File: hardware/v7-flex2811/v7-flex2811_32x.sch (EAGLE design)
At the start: 160 parts

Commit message: Rebuild a 32 strip from the slightly update single
Single has more room to place passives and slightly smaller
2818 pads so that there's more clearance with the edge
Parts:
- removed IN1: 4PAD, Sparky:4PAD
- added C21, C22, C23, C24, C25, C26, C27, C28, C29, C30, C31, C32: (no value), rcl:C-EUC0201
- added R61, R62, R63, R64, R65, R66, R67, R68, R69, R70, R71, R72, R73, R74, R75, R76, R77, R78, R79, R80, R81, R82, R83, R84, R85, R86, R87, R88, R89, R90, R91, R92, R93, R94, R95, R96: (no value), rcl:R-US_R0201
- added U$100, U$103, U$104, U$107, U$108, U$111, U$112, U$115, U$116, U$119, U$120, U$123, U$124, U$127, U$128, U$3, U$83, U$84, U$87, U$88, U$91, U$92, U$95, U$96, U$99: 4PAD, Sparky:4PAD
- added U$101, U$105, U$109, U$113, U$117, U$121, U$125, U$81, U$85, U$89, U$93, U$97: TP_4MM_MED_PAD, tom-tappytap-v5-flex:TP_4MM_MED_PAD
- added U$102, U$106, U$110, U$114, U$118, U$122, U$126, U$82, U$86, U$90, U$94, U$98: WS2818, Sparky:WS2818
- U$10, U$14, U$18, U$2, U$22, U$26, U$30, U$34, U$38, U$42, U$46, U$50, U$54, U$58, U$6, U$62, U$66, U$70, U$74, U$78: device adafruit:WS2818 -> Sparky:WS2818
- renumbered OUT1 to U$4
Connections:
- removed net BIN1: IN1.BIN, U$2.BIN
- removed net DIN1: IN1.DIN, R4.2, U$4.BIN, U$6.BIN, U$7.BIN
- new net BIN0: U$2.BIN, U$3.P$2
- new net DIN0: R4.2, U$3.P$1, U$4.P$2, U$6.BIN, U$7.P$2
- new net DOUT0: R1.2, R5.1, U$10.BIN, U$11.P$2, U$4.P$1, U$7.P$1, U$8.P$2
- new net DOUT21: R65.1, R67.2, U$88.P$1, U$91.P$1, U$92.P$2, U$94.BIN, U$95.P$2
- new net DOUT22: R68.1, R70.2, U$92.P$1, U$95.P$1, U$96.P$2, U$98.BIN, U$99.P$2
- new net DOUT23: R71.1, R73.2, U$100.P$2, U$102.BIN, U$103.P$2, U$96.P$1, U$99.P$1
- new net DOUT24: R74.1, R76.2, U$100.P$1, U$103.P$1, U$104.P$2, U$106.BIN, U$107.P$2
- new net DOUT25: R77.1, R79.2, U$104.P$1, U$107.P$1, U$108.P$2, U$110.BIN, U$111.P$2
- new net DOUT26: R80.1, R82.2, U$108.P$1, U$111.P$1, U$112.P$2, U$114.BIN, U$115.P$2
- new net DOUT27: R83.1, R85.2, U$112.P$1, U$115.P$1, U$116.P$2, U$118.BIN, U$119.P$2
- new net DOUT28: R86.1, R88.2, U$116.P$1, U$119.P$1, U$120.P$2, U$122.BIN, U$123.P$2
- new net DOUT29: R89.1, R91.2, U$120.P$1, U$123.P$1, U$124.P$2, U$126.BIN, U$127.P$2
- new net DOUT30: R92.1, R94.2, U$124.P$1, U$127.P$1, U$128.P$2
- new net DOUT31: R95.1, U$128.P$1
- new net N$61: R61.1, U$82.DIN
- new net N$62: R62.2, U$82.DO
- new net N$63: R63.1, U$82.VDD
- new net N$64: R64.1, U$86.DIN
- new net N$65: R65.2, U$86.DO
- new net N$66: R66.1, U$86.VDD
- new net N$67: R67.1, U$90.DIN
- new net N$68: R68.2, U$90.DO
- new net N$69: R69.1, U$90.VDD
- new net N$70: R70.1, U$94.DIN
- new net N$71: R71.2, U$94.DO
- new net N$72: R72.1, U$94.VDD
- new net N$73: R73.1, U$98.DIN
- new net N$74: R74.2, U$98.DO
- new net N$75: R75.1, U$98.VDD
- new net N$76: R76.1, U$102.DIN
- new net N$77: R77.2, U$102.DO
- new net N$78: R78.1, U$102.VDD
- new net N$79: R79.1, U$106.DIN
- new net N$80: R80.2, U$106.DO
- new net N$81: R81.1, U$106.VDD
- new net N$82: R82.1, U$110.DIN
- new net N$83: R83.2, U$110.DO
- new net N$84: R84.1, U$110.VDD
- new net N$85: R85.1, U$114.DIN
- new net N$86: R86.2, U$114.DO
- new net N$87: R87.1, U$114.VDD
- new net N$88: R88.1, U$118.DIN
- new net N$89: R89.2, U$118.DO
- new net N$90: R90.1, U$118.VDD
- new net N$91: R91.1, U$122.DIN
- new net N$92: R92.2, U$122.DO
- new net N$93: R93.1, U$122.VDD
- new net N$94: R94.1, U$126.DIN
- new net N$95: R95.2, U$126.DO
- new net N$96: R96.1, U$126.VDD
- new net NEG_PAD0: U$1.0, U$2.OUTB, U$2.OUTG, U$2.OUTR
- new net NEG_PAD21: U$85.0, U$86.OUTB, U$86.OUTG, U$86.OUTR
- new net NEG_PAD22: U$89.0, U$90.OUTB, U$90.OUTG, U$90.OUTR
- new net NEG_PAD23: U$93.0, U$94.OUTB, U$94.OUTG, U$94.OUTR
- new net NEG_PAD24: U$97.0, U$98.OUTB, U$98.OUTG, U$98.OUTR
- new net NEG_PAD25: U$101.0, U$102.OUTB, U$102.OUTG, U$102.OUTR
- new net NEG_PAD26: U$105.0, U$106.OUTB, U$106.OUTG, U$106.OUTR
- new net NEG_PAD27: U$109.0, U$110.OUTB, U$110.OUTG, U$110.OUTR
- new net NEG_PAD28: U$113.0, U$114.OUTB, U$114.OUTG, U$114.OUTR
- new net NEG_PAD29: U$117.0, U$118.OUTB, U$118.OUTG, U$118.OUTR
- new net NEG_PAD30: U$121.0, U$122.OUTB, U$122.OUTG, U$122.OUTR
- new net NEG_PAD31: U$125.0, U$126.OUTB, U$126.OUTG, U$126.OUTR
- net DOUT1: now also R2.1, R7.2, U$11.P$1, U$12.P$2, U$14.BIN, U$15.P$2, U$8.P$1; no longer R1.2, R5.1, U$10.BIN, U$11.BIN, U$4.DIN, U$7.DIN, U$8.BIN
- net DOUT10: now also R32.1, R34.2, U$44.P$1, U$47.P$1, U$48.P$2, U$50.BIN, U$51.P$2; no longer R29.1, R31.2, U$40.DIN, U$43.DIN, U$44.BIN, U$46.BIN, U$47.BIN
- net DOUT11: now also R35.1, R37.2, U$48.P$1, U$51.P$1, U$52.P$2, U$54.BIN, U$55.P$2; no longer R32.1, R34.2, U$44.DIN, U$47.DIN, U$48.BIN, U$50.BIN, U$51.BIN
- net DOUT12: now also R38.1, R40.2, U$52.P$1, U$55.P$1, U$56.P$2, U$58.BIN, U$59.P$2; no longer R35.1, R37.2, U$48.DIN, U$51.DIN, U$52.BIN, U$54.BIN, U$55.BIN
- net DOUT13: now also R41.1, R43.2, U$56.P$1, U$59.P$1, U$60.P$2, U$62.BIN, U$63.P$2; no longer R38.1, R40.2, U$52.DIN, U$55.DIN, U$56.BIN, U$58.BIN, U$59.BIN
- net DOUT14: now also R44.1, R46.2, U$60.P$1, U$63.P$1, U$64.P$2, U$66.BIN, U$67.P$2; no longer R41.1, R43.2, U$56.DIN, U$59.DIN, U$60.BIN, U$62.BIN, U$63.BIN
- net DOUT15: now also R47.1, R49.2, U$64.P$1, U$67.P$1, U$68.P$2, U$70.BIN, U$71.P$2; no longer R44.1, R46.2, U$60.DIN, U$63.DIN, U$64.BIN, U$66.BIN, U$67.BIN
- net DOUT16: now also R50.1, R52.2, U$68.P$1, U$71.P$1, U$72.P$2, U$74.BIN, U$75.P$2; no longer R47.1, R49.2, U$64.DIN, U$67.DIN, U$68.BIN, U$70.BIN, U$71.BIN
- net DOUT17: now also R53.1, R55.2, U$72.P$1, U$75.P$1, U$76.P$2, U$78.BIN, U$79.P$2; no longer R50.1, R52.2, U$68.DIN, U$71.DIN, U$72.BIN, U$74.BIN, U$75.BIN
- net DOUT18: now also R56.1, R58.2, U$76.P$1, U$79.P$1, U$80.P$2, U$82.BIN, U$83.P$2; no longer R53.1, R55.2, U$72.DIN, U$75.DIN, U$76.BIN, U$78.BIN, U$79.BIN
- net DOUT19: now also R59.1, R61.2, U$80.P$1, U$83.P$1, U$84.P$2, U$86.BIN, U$87.P$2; no longer R56.1, R58.2, U$76.DIN, U$79.DIN, U$80.BIN
- net DOUT2: now also R10.2, R8.1, U$12.P$1, U$15.P$1, U$16.P$2, U$18.BIN, U$19.P$2; no longer R2.1, R7.2, U$11.DIN, U$12.BIN, U$14.BIN, U$15.BIN, U$8.DIN
- net DOUT20: now also R62.1, R64.2, U$84.P$1, U$87.P$1, U$88.P$2, U$90.BIN, U$91.P$2; no longer R59.1, U$80.DIN
- net DOUT3: now also R11.1, R13.2, U$16.P$1, U$19.P$1, U$20.P$2, U$22.BIN, U$23.P$2; no longer R10.2, R8.1, U$12.DIN, U$15.DIN, U$16.BIN, U$18.BIN, U$19.BIN
- net DOUT4: now also R14.1, R16.2, U$20.P$1, U$23.P$1, U$24.P$2, U$26.BIN, U$27.P$2; no longer R11.1, R13.2, U$16.DIN, U$19.DIN, U$20.BIN, U$22.BIN, U$23.BIN
- net DOUT5: now also R17.1, R19.2, U$24.P$1, U$27.P$1, U$28.P$2, U$30.BIN, U$31.P$2; no longer R14.1, R16.2, U$20.DIN, U$23.DIN, U$24.BIN, U$26.BIN, U$27.BIN
- net DOUT6: now also R20.1, R22.2, U$28.P$1, U$31.P$1, U$32.P$2, U$34.BIN, U$35.P$2; no longer R17.1, R19.2, U$24.DIN, U$27.DIN, U$28.BIN, U$30.BIN, U$31.BIN
- net DOUT7: now also R23.1, R25.2, U$32.P$1, U$35.P$1, U$36.P$2, U$38.BIN, U$39.P$2; no longer R20.1, R22.2, U$28.DIN, U$31.DIN, U$32.BIN, U$34.BIN, U$35.BIN
- net DOUT8: now also R26.1, R28.2, U$36.P$1, U$39.P$1, U$40.P$2, U$42.BIN, U$43.P$2; no longer R23.1, R25.2, U$32.DIN, U$35.DIN, U$36.BIN, U$38.BIN, U$39.BIN
- net DOUT9: now also R29.1, R31.2, U$40.P$1, U$43.P$1, U$44.P$2, U$46.BIN, U$47.P$2; no longer R26.1, R28.2, U$36.DIN, U$39.DIN, U$40.BIN, U$42.BIN, U$43.BIN
- net GND: now also C21.2, C22.2, C23.2, C24.2, C25.2, C26.2, C27.2, C28.2, C29.2, C30.2, C31.2, C32.2, U$100.P$3, U$102.GND, U$103.P$3, U$104.P$3, U$106.GND, U$107.P$3, U$108.P$3, U$11.P$3, U$110.GND, U$111.P$3, U$112.P$3, U$114.GND, U$115.P$3, U$116.P$3, U$118.GND, U$119.P$3, U$12.P$3, U$120.P$3, U$122.GND, U$123.P$3, U$124.P$3, U$126.GND, U$127.P$3, U$128.P$3, U$15.P$3, U$16.P$3, U$19.P$3, U$20.P$3, U$23.P$3, U$24.P$3, U$27.P$3, U$28.P$3, U$3.P$3, U$31.P$3, U$32.P$3, U$35.P$3, U$36.P$3, U$39.P$3, U$4.P$3, U$40.P$3, U$43.P$3, U$44.P$3, U$47.P$3, U$48.P$3, U$51.P$3, U$52.P$3, U$55.P$3, U$56.P$3, U$59.P$3, U$60.P$3, U$63.P$3, U$64.P$3, U$67.P$3, U$68.P$3, U$7.P$3, U$71.P$3, U$72.P$3, U$75.P$3, U$76.P$3, U$79.P$3, U$8.P$3, U$80.P$3, U$82.GND, U$83.P$3, U$84.P$3, U$86.GND, U$87.P$3, U$88.P$3, U$90.GND, U$91.P$3, U$92.P$3, U$94.GND, U$95.P$3, U$96.P$3, U$98.GND, U$99.P$3; no longer IN1.GND, U$11.GND, U$12.GND, U$15.GND, U$16.GND, U$19.GND, U$20.GND, U$23.GND, U$24.GND, U$27.GND, U$28.GND, U$31.GND, U$32.GND, U$35.GND, U$36.GND, U$39.GND, U$4.GND, U$40.GND, U$43.GND, U$44.GND, U$47.GND, U$48.GND, U$51.GND, U$52.GND, U$55.GND, U$56.GND, U$59.GND, U$60.GND, U$63.GND, U$64.GND, U$67.GND, U$68.GND, U$7.GND, U$71.GND, U$72.GND, U$75.GND, U$76.GND, U$79.GND, U$8.GND, U$80.GND
- net NEG_PAD1: now also U$5.0, U$6.OUTB, U$6.OUTG, U$6.OUTR; no longer U$1.0, U$2.OUTB, U$2.OUTG, U$2.OUTR
- net NEG_PAD10: now also U$41.0, U$42.OUTB, U$42.OUTG, U$42.OUTR; no longer U$37.0, U$38.OUTB, U$38.OUTG, U$38.OUTR
- net NEG_PAD11: now also U$45.0, U$46.OUTB, U$46.OUTG, U$46.OUTR; no longer U$41.0, U$42.OUTB, U$42.OUTG, U$42.OUTR
- net NEG_PAD12: now also U$49.0, U$50.OUTB, U$50.OUTG, U$50.OUTR; no longer U$45.0, U$46.OUTB, U$46.OUTG, U$46.OUTR
- net NEG_PAD13: now also U$53.0, U$54.OUTB, U$54.OUTG, U$54.OUTR; no longer U$49.0, U$50.OUTB, U$50.OUTG, U$50.OUTR
- net NEG_PAD14: now also U$57.0, U$58.OUTB, U$58.OUTG, U$58.OUTR; no longer U$53.0, U$54.OUTB, U$54.OUTG, U$54.OUTR
- net NEG_PAD15: now also U$61.0, U$62.OUTB, U$62.OUTG, U$62.OUTR; no longer U$57.0, U$58.OUTB, U$58.OUTG, U$58.OUTR
- net NEG_PAD16: now also U$65.0, U$66.OUTB, U$66.OUTG, U$66.OUTR; no longer U$61.0, U$62.OUTB, U$62.OUTG, U$62.OUTR
- net NEG_PAD17: now also U$69.0, U$70.OUTB, U$70.OUTG, U$70.OUTR; no longer U$65.0, U$66.OUTB, U$66.OUTG, U$66.OUTR
- net NEG_PAD18: now also U$73.0, U$74.OUTB, U$74.OUTG, U$74.OUTR; no longer U$69.0, U$70.OUTB, U$70.OUTG, U$70.OUTR
- net NEG_PAD19: now also U$77.0, U$78.OUTB, U$78.OUTG, U$78.OUTR; no longer U$73.0, U$74.OUTB, U$74.OUTG, U$74.OUTR
- net NEG_PAD2: now also U$10.OUTB, U$10.OUTG, U$10.OUTR, U$9.0; no longer U$5.0, U$6.OUTB, U$6.OUTG, U$6.OUTR
- net NEG_PAD20: now also U$81.0, U$82.OUTB, U$82.OUTG, U$82.OUTR; no longer U$77.0, U$78.OUTB, U$78.OUTG, U$78.OUTR
- net NEG_PAD3: now also U$13.0, U$14.OUTB, U$14.OUTG, U$14.OUTR; no longer U$10.OUTB, U$10.OUTG, U$10.OUTR, U$9.0
- net NEG_PAD4: now also U$17.0, U$18.OUTB, U$18.OUTG, U$18.OUTR; no longer U$13.0, U$14.OUTB, U$14.OUTG, U$14.OUTR
- net NEG_PAD5: now also U$21.0, U$22.OUTB, U$22.OUTG, U$22.OUTR; no longer U$17.0, U$18.OUTB, U$18.OUTG, U$18.OUTR
- net NEG_PAD6: now also U$25.0, U$26.OUTB, U$26.OUTG, U$26.OUTR; no longer U$21.0, U$22.OUTB, U$22.OUTG, U$22.OUTR
- net NEG_PAD7: now also U$29.0, U$30.OUTB, U$30.OUTG, U$30.OUTR; no longer U$25.0, U$26.OUTB, U$26.OUTG, U$26.OUTR
- net NEG_PAD8: now also U$33.0, U$34.OUTB, U$34.OUTG, U$34.OUTR; no longer U$29.0, U$30.OUTB, U$30.OUTG, U$30.OUTR
- net NEG_PAD9: now also U$37.0, U$38.OUTB, U$38.OUTG, U$38.OUTR; no longer U$33.0, U$34.OUTB, U$34.OUTG, U$34.OUTR
- net VCC: now also C21.1, C22.1, C23.1, C24.1, C25.1, C26.1, C27.1, C28.1, C29.1, C30.1, C31.1, C32.1, R63.2, R66.2, R69.2, R72.2, R75.2, R78.2, R81.2, R84.2, R87.2, R90.2, R93.2, R96.2, U$100.P$4, U$101.1, U$103.P$4, U$104.P$4, U$105.1, U$107.P$4, U$108.P$4, U$109.1, U$11.P$4, U$111.P$4, U$112.P$4, U$113.1, U$115.P$4, U$116.P$4, U$117.1, U$119.P$4, U$12.P$4, U$120.P$4, U$121.1, U$123.P$4, U$124.P$4, U$125.1, U$127.P$4, U$128.P$4, U$15.P$4, U$16.P$4, U$19.P$4, U$20.P$4, U$23.P$4, U$24.P$4, U$27.P$4, U$28.P$4, U$3.P$4, U$31.P$4, U$32.P$4, U$35.P$4, U$36.P$4, U$39.P$4, U$4.P$4, U$40.P$4, U$43.P$4, U$44.P$4, U$47.P$4, U$48.P$4, U$51.P$4, U$52.P$4, U$55.P$4, U$56.P$4, U$59.P$4, U$60.P$4, U$63.P$4, U$64.P$4, U$67.P$4, U$68.P$4, U$7.P$4, U$71.P$4, U$72.P$4, U$75.P$4, U$76.P$4, U$79.P$4, U$8.P$4, U$80.P$4, U$81.1, U$83.P$4, U$84.P$4, U$85.1, U$87.P$4, U$88.P$4, U$89.1, U$91.P$4, U$92.P$4, U$93.1, U$95.P$4, U$96.P$4, U$97.1, U$99.P$4; no longer IN1.VCC, U$11.VCC, U$12.VCC, U$15.VCC, U$16.VCC, U$19.VCC, U$20.VCC, U$23.VCC, U$24.VCC, U$27.VCC, U$28.VCC, U$31.VCC, U$32.VCC, U$35.VCC, U$36.VCC, U$39.VCC, U$4.VCC, U$40.VCC, U$43.VCC, U$44.VCC, U$47.VCC, U$48.VCC, U$51.VCC, U$52.VCC, U$55.VCC, U$56.VCC, U$59.VCC, U$60.VCC, U$63.VCC, U$64.VCC, U$67.VCC, U$68.VCC, U$7.VCC, U$71.VCC, U$72.VCC, U$75.VCC, U$76.VCC, U$79.VCC, U$8.VCC, U$80.VCC

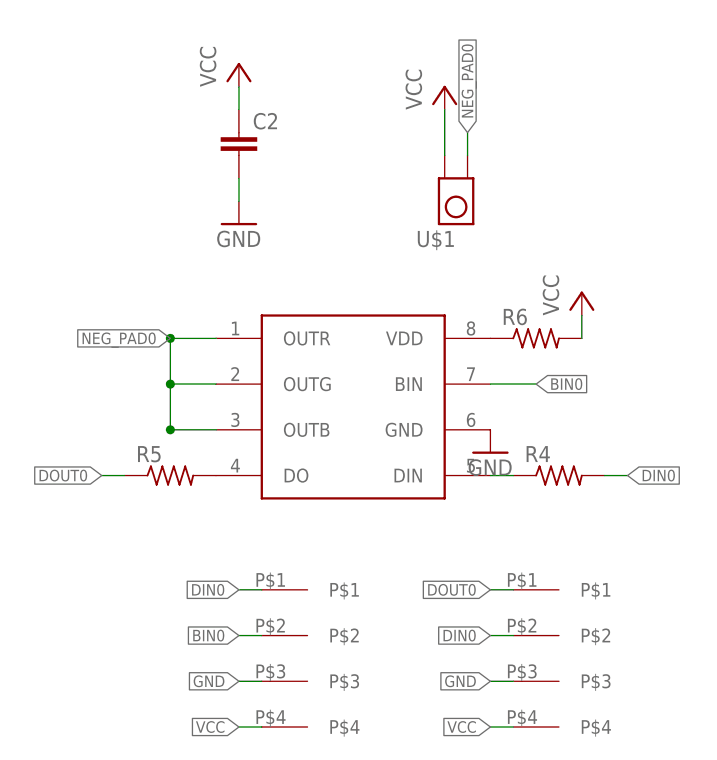
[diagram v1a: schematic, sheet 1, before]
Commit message: More edit for manufacturability
Add a preliminary BOM
Add labels for the ICs for assembly
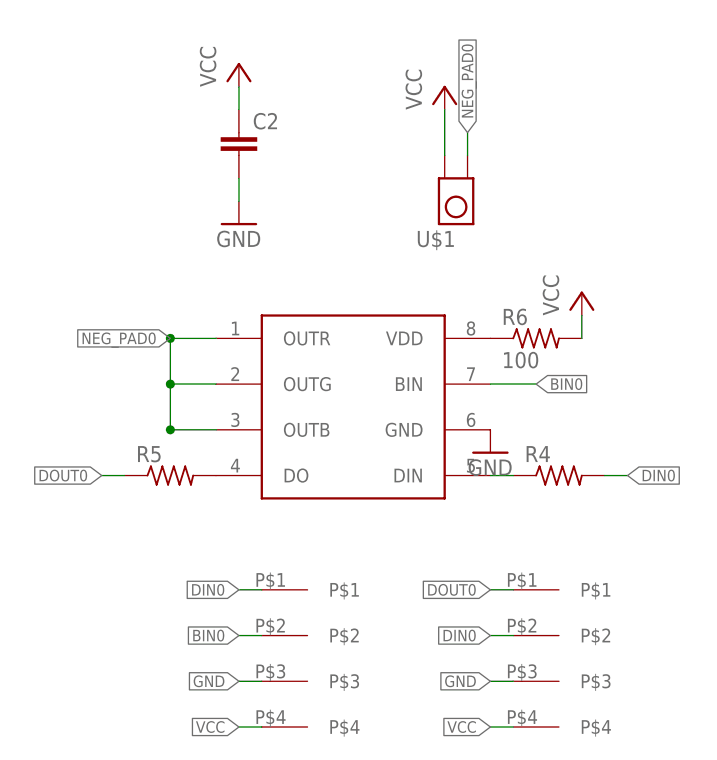
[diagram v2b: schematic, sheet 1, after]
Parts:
- R12, R15, R18, R21, R24, R27, R3, R30, R33, R36, R39, R42, R45, R48, R51, R54, R57, R6, R60, R63, R66, R69, R72, R75, R78, R81, R84, R87, R9, R90, R93, R96: value (none) -> 100
- renumbered U$10 to U3, U$102 to U26, U$106 to U27, U$110 to U28, U$114 to U29, U$118 to U30, U$122 to U31, U$126 to U32, U$14 to U4, U$18 to U5, U$2 to U1, U$22 to U6, U$26 to U7, U$30 to U8, U$34 to U9, U$38 to U10, U$42 to U11, U$46 to U12, U$50 to U13, U$54 to U14, U$58 to U15, U$6 to U2, U$62 to U16, U$66 to U17, U$70 to U18, U$74 to U19, U$78 to U20, U$82 to U21, U$86 to U22, U$90 to U23, U$94 to U24, U$98 to U25
